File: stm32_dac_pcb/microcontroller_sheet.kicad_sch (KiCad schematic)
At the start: 22 parts, among them J1 Conn_01x03, J2 Conn_01x05, J3 USB_C_Receptacle_USB2.0, SW1 SW_Push, SW2 SW_Push, U3 STM32F411CEUx, Y1 25MHz, 9pF

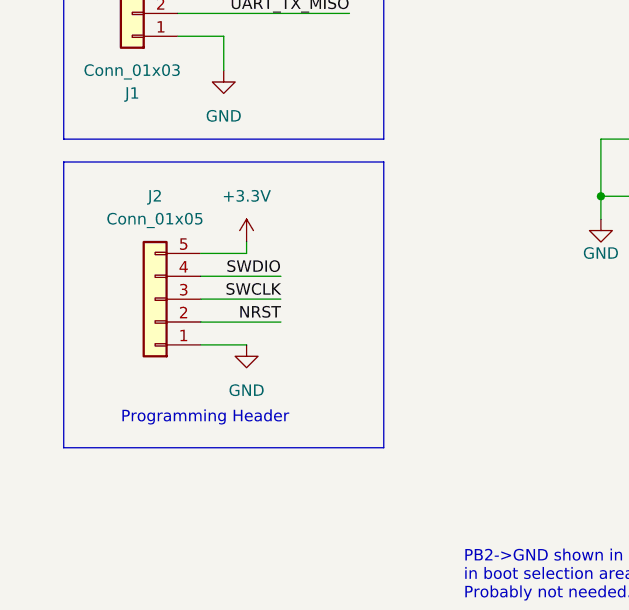
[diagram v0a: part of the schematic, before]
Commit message: Convert to SOICbite SWD+UART connector for Rev 3
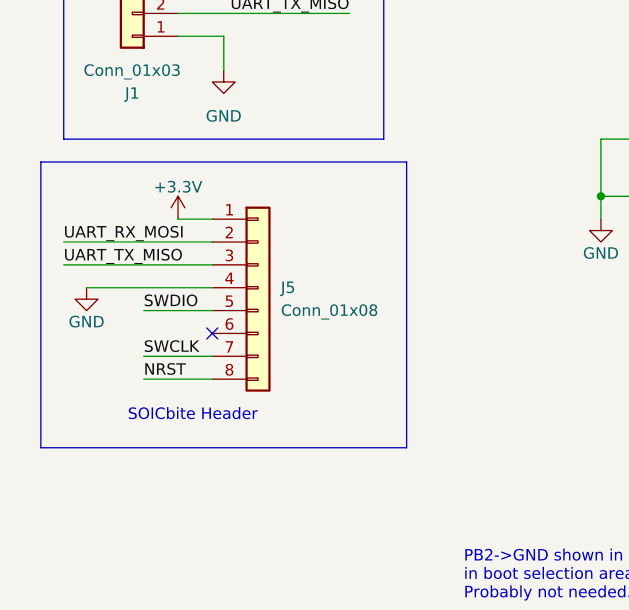
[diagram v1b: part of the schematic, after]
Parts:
- removed J2: Conn_01x05, Connector_PinHeader_2.00mm:PinHeader_1x05_P2.00mm_Vertical, symbol Connector_Generic:Conn_01x05
- added J5: Conn_01x08, 0_project_fp_lib:SOIC_clipProgSmall, symbol Connector_Generic:Conn_01x08
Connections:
- net +3.3V: now also J5.1 (Pin_1)
- net GND: now also J5.4 (Pin_4)
- net NRST: now also J5.8 (Pin_8)
- net SWCLK: now also J5.7 (Pin_7)
- net SWDIO: now also J5.5 (Pin_5)
- net UART_RX_MOSI: now also J5.2 (Pin_2)
- net UART_TX_MISO: now also J5.3 (Pin_3)
- no-connect marks 22 -> 23
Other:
- note added: "SOICbite Header"
- note removed: "Programming Header"
